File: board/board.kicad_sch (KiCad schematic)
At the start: 22 parts, among them J1 UART, J2 008_USB, J3 DebugEdge_02x05, J4 019_100BASE-T_with_CT, J5 ADC_2x3, J6 SWD_6_Pol_Needle, J7 SPI_2x3, J8 I2C_2x2, J9 UART_2x2, SW1 PTS636 SK25J SMTR LFS

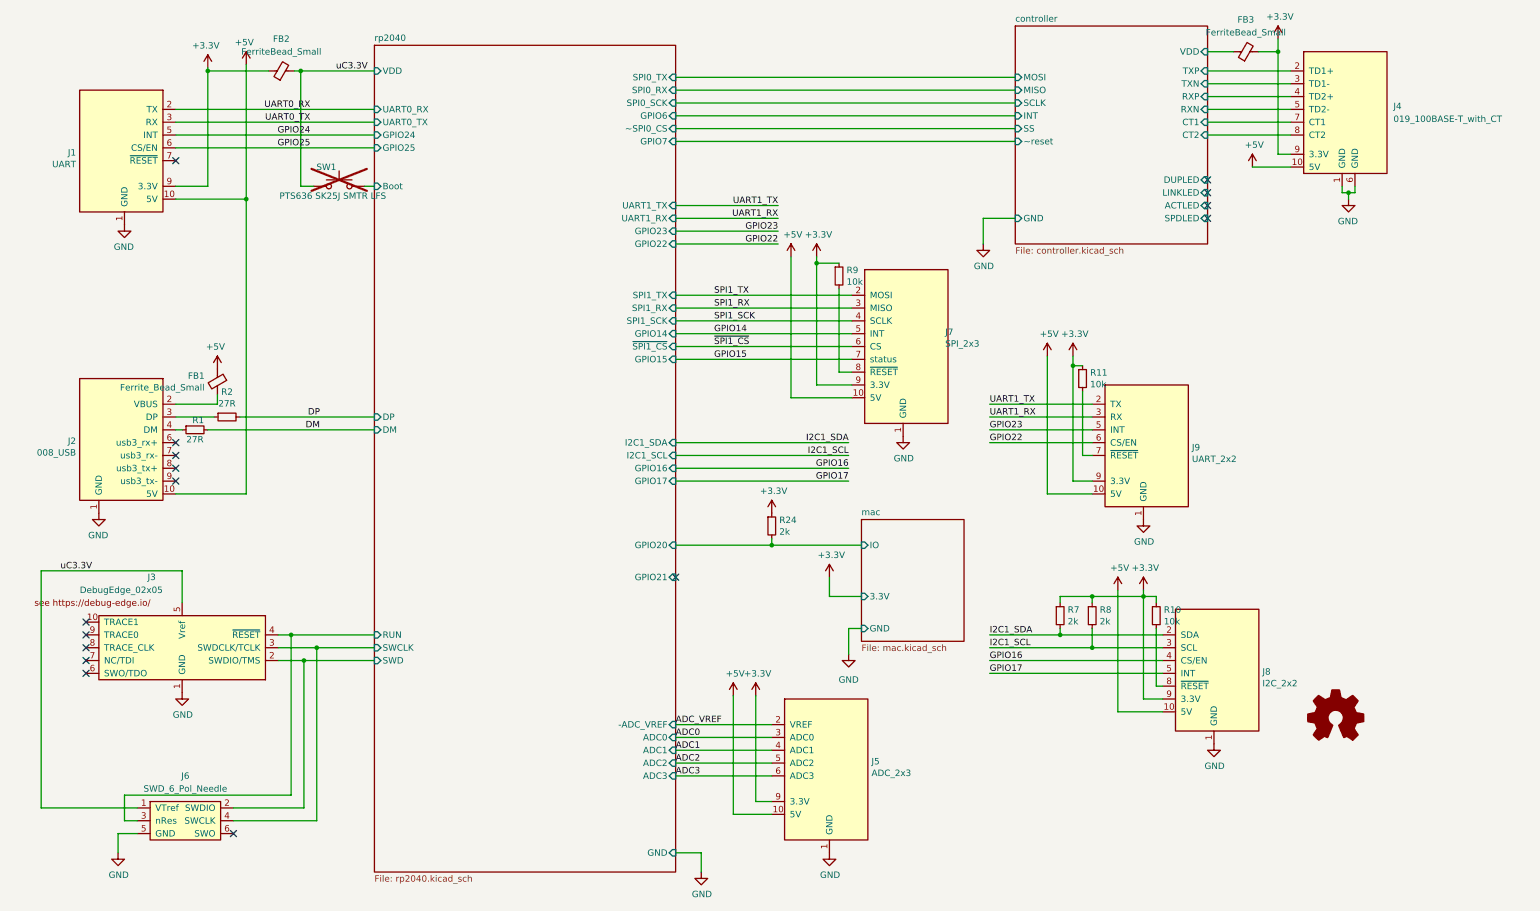
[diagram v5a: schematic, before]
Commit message: fixed I2C pinning defect
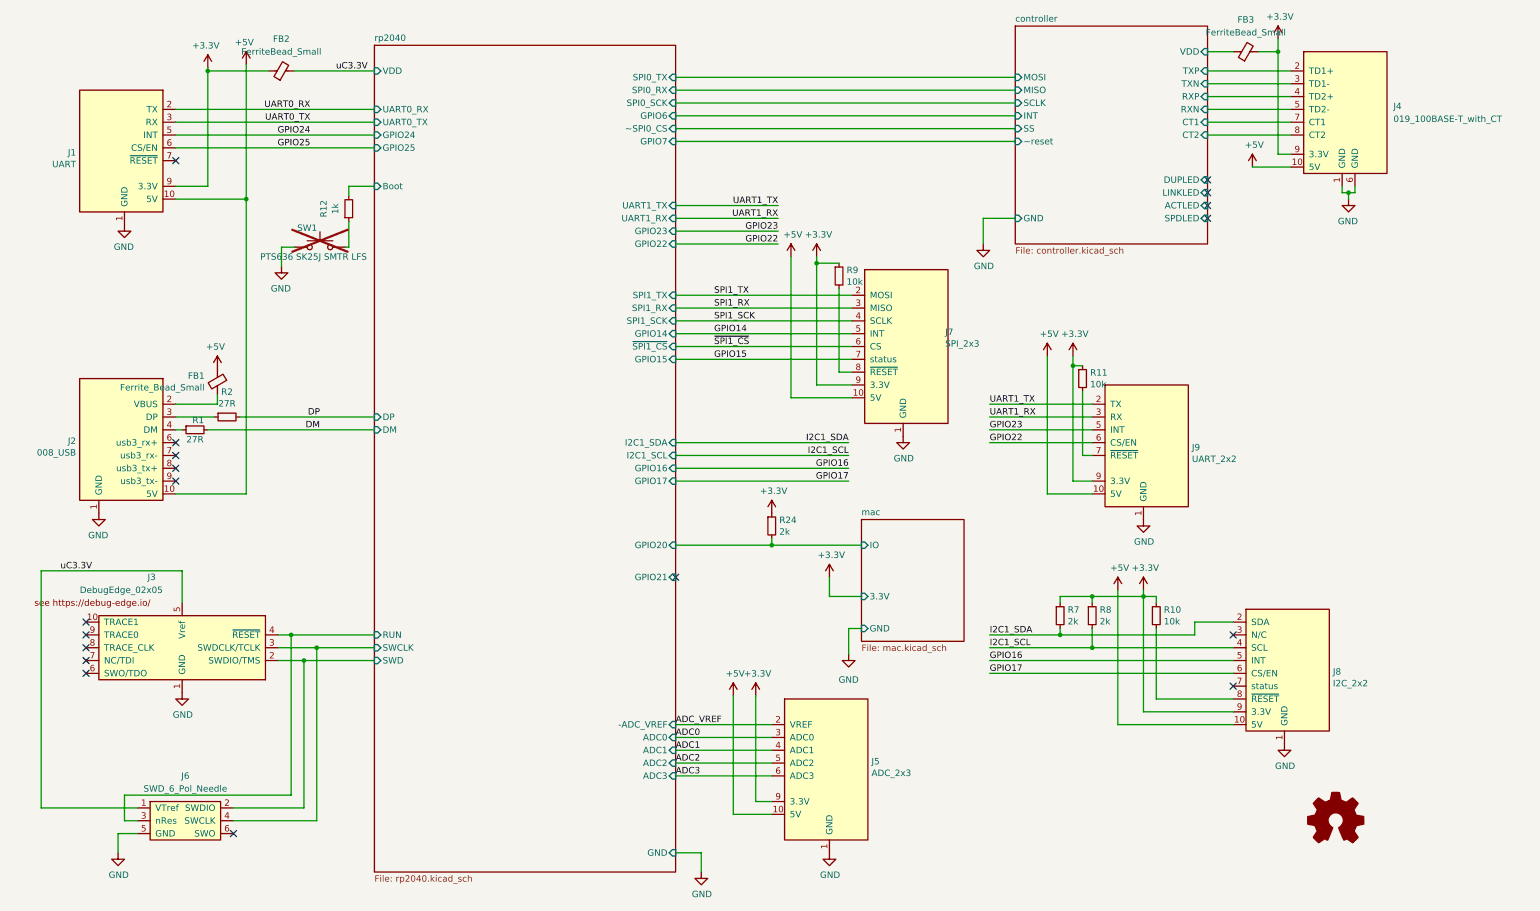
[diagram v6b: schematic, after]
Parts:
- added R12: 1k, Resistor_SMD:R_0603_1608Metric, symbol Device:R_Small
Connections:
- net GND: now also SW1.1
- net GPIO16: now also J8.5 (INT); no longer J8.4 (CS/EN)
- net GPIO17: now also J8.6 (CS/EN); no longer J8.5 (INT)
- net I2C1_SCL: now also J8.4 (SCL); no longer J8.3 (SCL)
- net rp2040/Boot: now also R12.2; no longer SW1.2
- net uC3.3V: no longer SW1.1
- new net: R12.1, SW1.2
- no-connect marks 16 -> 18
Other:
- moved on the sheet: SW1

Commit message: moved all components to top layer
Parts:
- FB2, FB3: footprint Inductor_SMD:L_0603_1608Metric -> Inductor_SMD:L_0805_2012Metric
- R10, R11, R24, R7, R8, R9: footprint Resistor_SMD:R_0603_1608Metric -> Resistor_SMD:R_0402_1005Metric
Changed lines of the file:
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@@
       (effects (font (size 1.27 1.27)) (justify left))
     )
-    (property "Footprint" "Resistor_SMD:R_0603_1608Metric" (at 222.885 86.36 0)
+    (property "Footprint" "Resistor_SMD:R_0402_1005Metric" (at 222.885 86.36 0)
       (effects (font (size 1.27 1.27)) hide)
     )
@@
       (effects (font (size 1.27 1.27)) (justify left))
     )
-    (property "Footprint" "Resistor_SMD:R_0603_1608Metric" (at 161.29 115.57 0)
+    (property "Footprint" "Resistor_SMD:R_0402_1005Metric" (at 161.29 115.57 0)
       (effects (font (size 1.27 1.27)) hide)
     )
@@
       (effects (font (size 1.27 1.27)) (justify left))
     )
-    (property "Footprint" "Resistor_SMD:R_0603_1608Metric" (at 218.44 133.35 0)
+    (property "Footprint" "Resistor_SMD:R_0402_1005Metric" (at 218.44 133.35 0)
       (effects (font (size 1.27 1.27)) hide)
     )
@@
       (effects (font (size 1.27 1.27)) (justify left))
     )
-    (property "Footprint" "Resistor_SMD:R_0603_1608Metric" (at 237.49 133.35 0)
+    (property "Footprint" "Resistor_SMD:R_0402_1005Metric" (at 237.49 133.35 0)
       (effects (font (size 1.27 1.27)) hide)
     )
@@
       (effects (font (size 1.27 1.27)))
     )
-    (property "Footprint" "Inductor_SMD:L_0603_1608Metric" (at 255.27 23.368 90)
+    (property "Footprint" "Inductor_SMD:L_0805_2012Metric" (at 255.27 23.368 90)
       (effects (font (size 1.27 1.27)) hide)
     )
@@
       (effects (font (size 1.27 1.27)))
     )
-    (property "Footprint" "Inductor_SMD:L_0603_1608Metric" (at 64.135 27.178 90)
+    (property "Footprint" "Inductor_SMD:L_0805_2012Metric" (at 64.135 27.178 90)
       (effects (font (size 1.27 1.27)) hide)
     )
@@
       (effects (font (size 1.27 1.27)) (justify left))
     )
-    (property "Footprint" "Resistor_SMD:R_0603_1608Metric" (at 224.79 133.35 0)
+    (property "Footprint" "Resistor_SMD:R_0402_1005Metric" (at 224.79 133.35 0)
       (effects (font (size 1.27 1.27)) hide)
     )
@@
       (effects (font (size 1.27 1.27)) (justify left))
     )
-    (property "Footprint" "Resistor_SMD:R_0603_1608Metric" (at 174.625 66.04 0)
-      (effects (font (size 1.27 1.27)) hide)
-    )
+    (property "Footprint" "Resistor_SMD:R_0402_1005Metric" (at 174.625 66.04 0)
+      (effects (font (size 1.27 1.27)) hide)
+    )

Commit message: added lcsc part numbers
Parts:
- FB1, FB2, FB3: lcsc (none) -> C74764
- R1, R2: lcsc (none) -> C23345
- R10, R11, R9: lcsc (none) -> C25744
- R12: lcsc (none) -> C21190
- R24, R7, R8: lcsc (none) -> C4109
- SW1: lcsc (none) -> C2800965
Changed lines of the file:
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@@
+      (effects (font (size 1.27 1.27)) hide)
+    )
+    (property "lcsc" "" (at 236.22 100.33 0)
       (effects (font (size 1.27 1.27)) hide)
     )
@@
     )
     (property "Datasheet" "" (at 194.945 60.96 0)
+      (effects (font (size 1.27 1.27)) hide)
+    )
+    (property "lcsc" "" (at 187.325 77.47 0)
       (effects (font (size 1.27 1.27)) hide)
     )
@@
       (effects (font (size 1.27 1.27)) hide)
     )
+    (property "lcsc" "C25744" (at 222.885 86.36 0)
+      (effects (font (size 1.27 1.27)) hide)
+    )
     (pin "1")
     (pin "2")
@@
       (effects (font (size 1.27 1.27)) hide)
     )
+    (property "lcsc" "C23345" (at 46.99 96.52 0)
+      (effects (font (size 1.27 1.27)) hide)
+    )
     (pin "1")
     (pin "2")
@@
       (effects (font (size 1.27 1.27)) hide)
     )
+    (property "lcsc" "C4109" (at 161.29 115.57 0)
+      (effects (font (size 1.27 1.27)) hide)
+    )
     (pin "1")
     (pin "2")
@@
     )
     (property "Datasheet" "" (at 24.13 25.4 0)
+      (effects (font (size 1.27 1.27)) hide)
+    )
+    (property "lcsc" "" (at 31.75 41.91 0)
       (effects (font (size 1.27 1.27)) hide)
     )
@@
       (effects (font (size 1.27 1.27)) hide)
     )
+    (property "lcsc" "C4109" (at 218.44 133.35 0)
+      (effects (font (size 1.27 1.27)) hide)
+    )
     (pin "1")
     (pin "2")
@@
     )
     (property "Datasheet" "~" (at 237.49 133.35 0)
+      (effects (font (size 1.27 1.27)) hide)
+    )
+    (property "lcsc" "C25744" (at 237.49 133.35 0)
       (effects (font (size 1.27 1.27)) hide)
     )
@@
       (effects (font (size 1.27 1.27)) hide)
     )
+    (property "lcsc" "C2800965" (at 71.755 60.325 0)
+      (effects (font (size 1.27 1.27)) hide)
+    )
     (pin "1")
     (pin "2")
@@
     )
     (property "Datasheet" "~" (at 77.47 52.705 0)
+      (effects (font (size 1.27 1.27)) hide)
+    )
+    (property "lcsc" "C21190" (at 77.47 52.705 0)
       (effects (font (size 1.27 1.27)) hide)
     )
@@
       (effects (font (size 1.27 1.27)) hide)
     )
+    (property "lcsc" "C74764" (at 255.27 21.59 0)
+      (effects (font (size 1.27 1.27)) hide)
+    )
     (pin "1")
     (pin "2")
@@
       (effects (font (size 1.27 1.27)) hide)
     )
+    (property "lcsc" "C74764" (at 64.135 25.4 0)
+      (effects (font (size 1.27 1.27)) hide)
+    )
     (pin "1")
     (pin "2")
@@
     )
     (property "Datasheet" "" (at 44.45 149.86 0)
+      (effects (font (size 1.27 1.27)) hide)
+    )
+    (property "lcsc" "" (at 44.45 139.7 0)
       (effects (font (size 1.27 1.27)) hide)
     )
@@
       (effects (font (size 1.27 1.27)) hide)
     )
+    (property "lcsc" "" (at 172.72 162.56 0)
+      (effects (font (size 1.27 1.27)) hide)
+    )
     (pin "1")
     (pin "10")
@@
       (effects (font (size 1.27 1.27)) hide)
     )
+    (property "lcsc" "C23345" (at 53.34 93.98 0)
+      (effects (font (size 1.27 1.27)) hide)
+    )
     (pin "1")
     (pin "2")
@@
     )
     (property "Datasheet" "" (at 271.78 128.27 0)
+      (effects (font (size 1.27 1.27)) hide)
+    )
+    (property "lcsc" "" (at 264.16 144.78 0)
       (effects (font (size 1.27 1.27)) hide)
     )
@@
       (effects (font (size 1.27 1.27)) hide)
     )
+    (property "lcsc" "" (at 44.45 173.99 0)
+      (effects (font (size 1.27 1.27)) hide)
+    )
     (pin "1")
     (pin "2")
@@
       (effects (font (size 1.27 1.27)) hide)
     )
+    (property "lcsc" "" (at 273.05 173.99 0)
+      (effects (font (size 1.27 1.27)) hide)
+    )
     (instances
       (project "board"
@@
     )
     (property "Datasheet" "" (at 283.21 17.78 0)
+      (effects (font (size 1.27 1.27)) hide)
+    )
+    (property "lcsc" "" (at 275.59 34.29 0)
       (effects (font (size 1.27 1.27)) hide)
     )
@@
       (effects (font (size 1.27 1.27)) hide)
     )
+    (property "lcsc" "C4109" (at 224.79 133.35 0)
+      (effects (font (size 1.27 1.27)) hide)
+    )
     (pin "1")
     (pin "2")
@@
       (effects (font (size 1.27 1.27)) hide)
     )
+    (property "lcsc" "C74764" (at 51.435 86.995 0)
+      (effects (font (size 1.27 1.27)) hide)
+    )
     (pin "1")
     (pin "2")
@@
     )
     (property "Datasheet" "" (at 24.13 82.55 0)
+      (effects (font (size 1.27 1.27)) hide)
+    )
+    (property "lcsc" "" (at 31.75 99.06 0)
       (effects (font (size 1.27 1.27)) hide)
     )
@@
       (effects (font (size 1.27 1.27)) hide)
     )
+    (property "lcsc" "C25744" (at 174.625 66.04 0)
+      (effects (font (size 1.27 1.27)) hide)
+    )
